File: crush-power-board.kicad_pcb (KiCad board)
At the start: 4 copper layers, 101.4 x 117.1 mm, 105 parts, among them J1 XT90PW-F, J2 1x2 Header, J3 Molex Micro Fit 3.0, J4 Barrel_Jack, J5 2157601008, U1 BD9G341AEFJ, U2 SIC461ED-T1-GE3, U3 SIC461ED-T1-GE3, U4 BD9G341AEFJ

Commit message: 3v3_t routing
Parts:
- moved R34 32.2 mm to (18.8, 41.1)
- moved R33 30.6 mm to (17.1, 42.8), turned to 0 degrees
- moved R35 28.8 mm to (19.9, 43.6), turned to 90 degrees
- moved C48 27.8 mm to (21.4, 68.8), turned to 90 degrees
- moved R38 25.1 mm to (31.3, 46.0), turned to 0 degrees
- moved R37 24.9 mm to (26.7, 44.6), turned to 180 degrees
- moved C46 22.9 mm to (17.1, 48.8), turned to 180 degrees
- moved R36 22.4 mm to (31.3, 47.6), turned to 0 degrees
- moved C45 20.8 mm to (16.4, 51.2), turned to -90 degrees
- moved L4 20.1 mm to (28.7, 66.3), turned to -90 degrees
- moved C47 19.6 mm to (28.1, 47.6), turned to 0 degrees
- moved U4 18.2 mm to (22.6, 48.2), turned to 180 degrees
- moved D6 3.73 mm to (25.8, 55.2), turned to 180 degrees
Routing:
- net +BATT_T: track 3.69 -> 65.0 mm, vias 0 -> 1
- net 3V3_T: track 47.1 -> 33.9 mm
- net Net-(D5-K): track 30.8 -> 18.0 mm
- net Net-(D6-K): track 30.6 -> 17.8 mm
- net Net-(U4-EN): track 0.36 -> 7.89 mm
- net GND1: track 0.00 -> 7.03 mm, vias 8 -> 9
- net 5V: vias 133 -> 127
- added copper zone on F.Cu, net +BATT_T
- added copper zone on F.Cu, net 3V3_T
- added copper zone on B.Cu, net GND1
- added copper zone on In1.Cu, net GND1
- added copper zone on In2.Cu, net GND1
- added copper zone on F.Cu, net Net-(D6-K)

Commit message: misc design fixes
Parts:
- moved R34 0.60 mm to (18.8, 40.5)
- moved C15 0.60 mm to (88.2, 34.2)
- moved C13 0.20 mm to (59.2, 63.1)
- moved R18 0.20 mm to (59.2, 60.5)
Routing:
- net 12V: track 201.2 -> 190.5 mm, vias 157 -> 247
- net Net-(U4-EN): track 7.89 -> 8.56 mm
- net GND: vias 1322 -> 1302
- net 5V: vias 127 -> 232
- net 3V3: vias 2 -> 52
- added copper zone on B.Cu, net 3V3

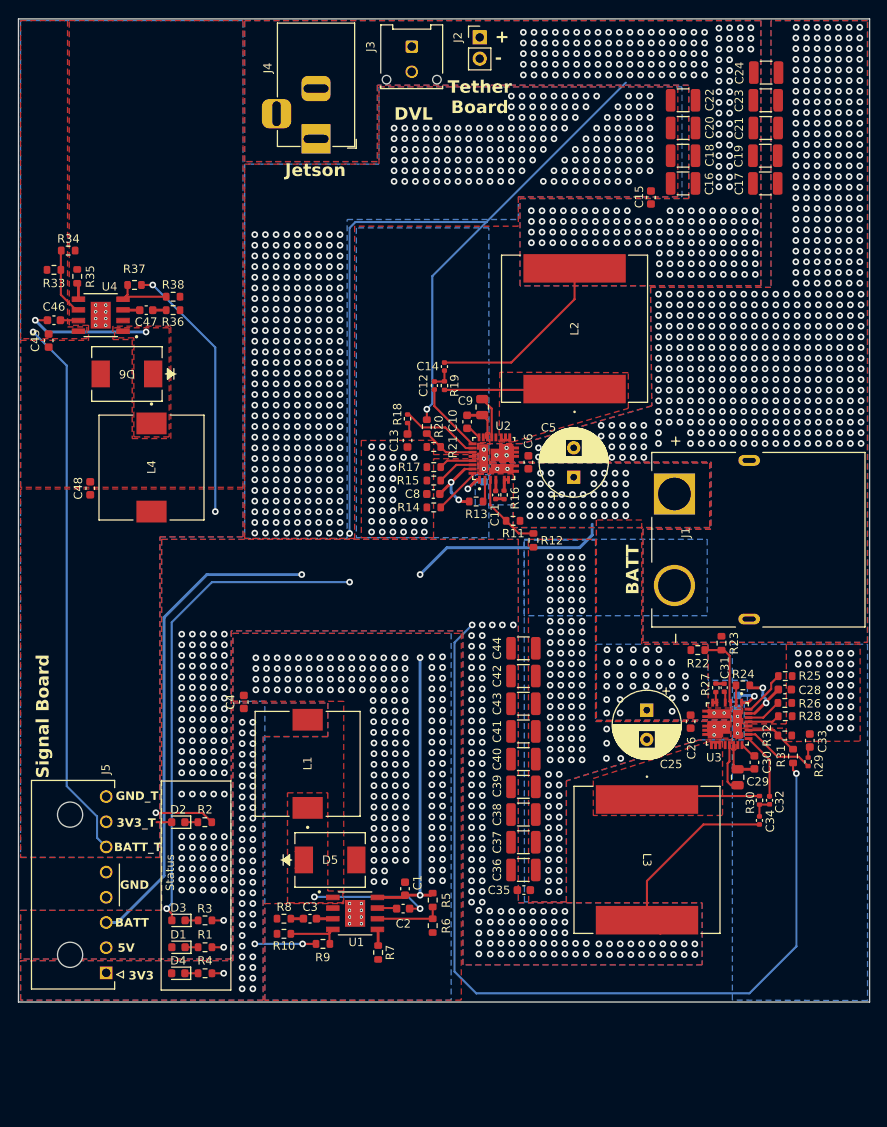
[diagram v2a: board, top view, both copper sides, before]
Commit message: fix silkscreen drc violations
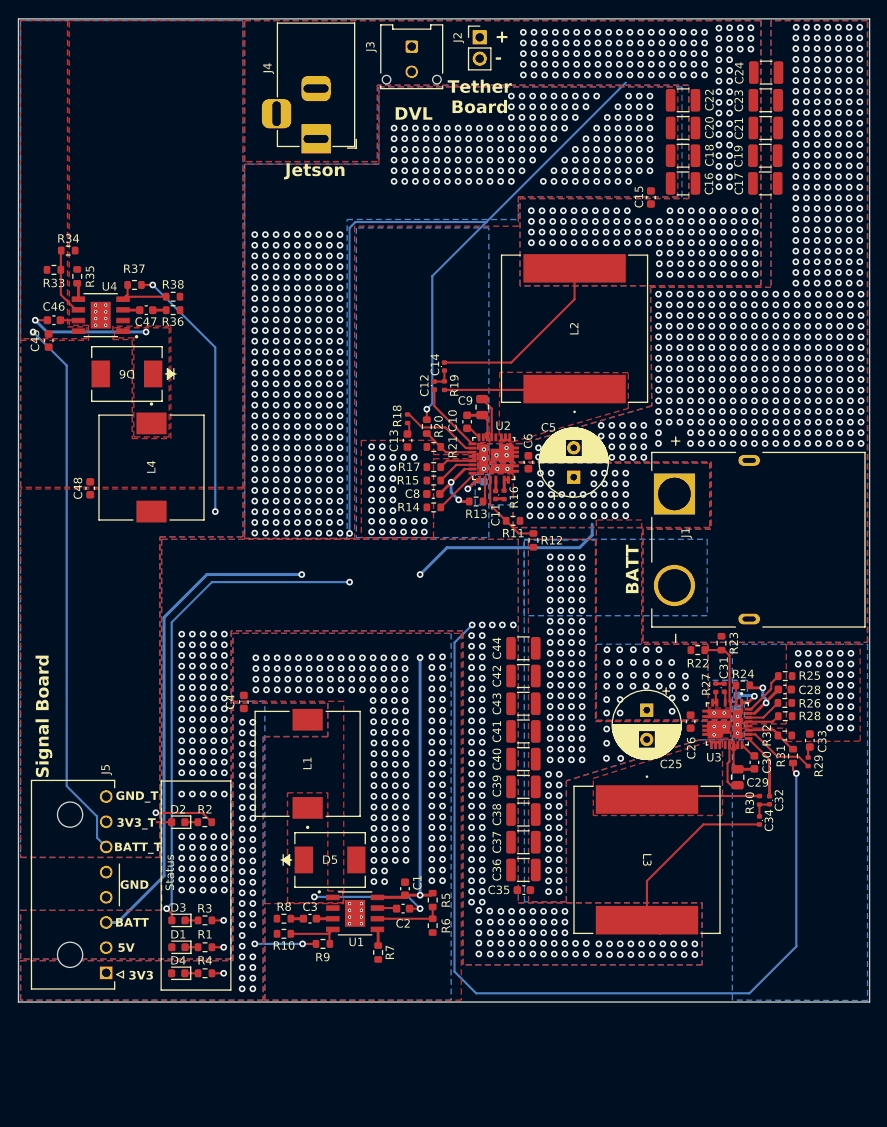
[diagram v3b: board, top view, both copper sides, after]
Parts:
- C11, C12, C14, C31, C32, C34: footprint Capacitor_SMD:C_0402_1005Metric -> crush-power-footprints:C_0402_1005Metric
- J4: footprint Connector_BarrelJack:BarrelJack_Horizontal -> crush-power-footprints:BarrelJack_Horizontal
- R16, R18, R19, R27, R29, R30: footprint Resistor_SMD:R_0402_1005Metric -> crush-power-footprints:R_0402_1005Metric
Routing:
- net Net-(U3-VSNS): track 8.11 -> 12.3 mm

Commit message: update board size
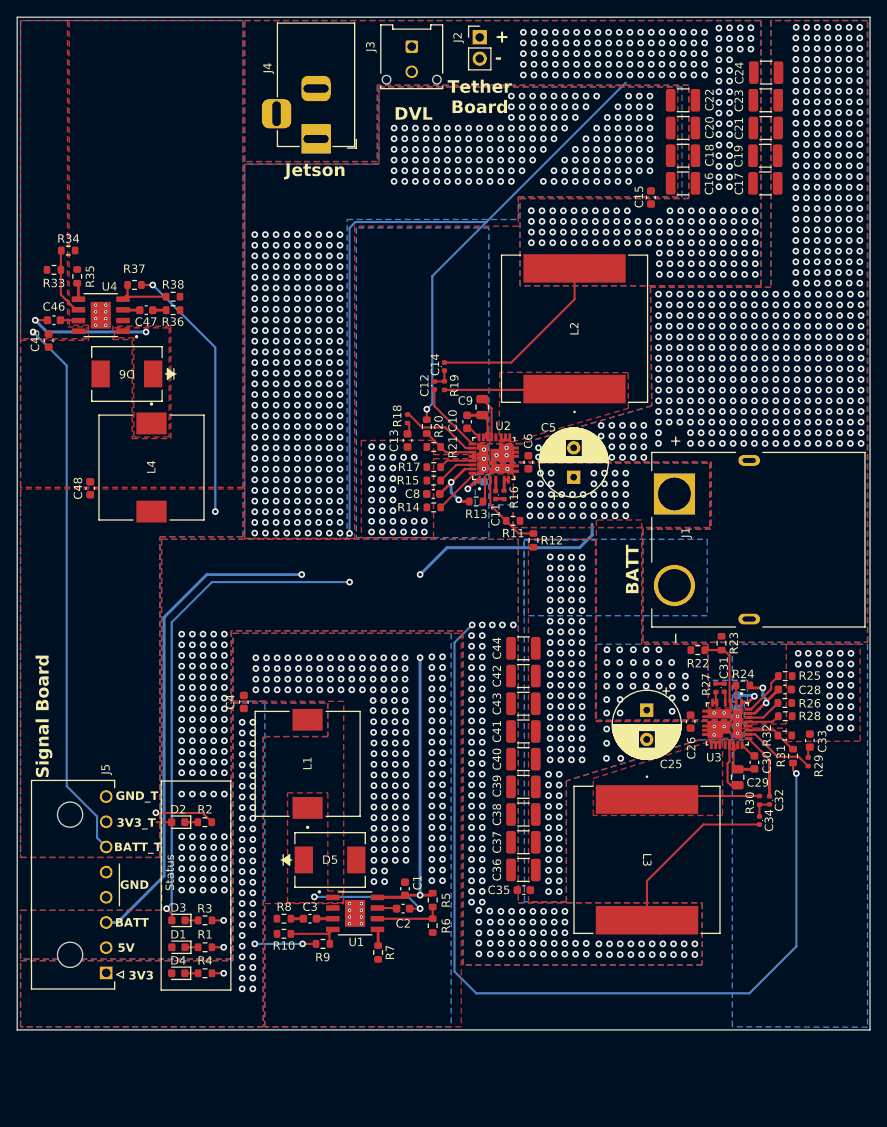
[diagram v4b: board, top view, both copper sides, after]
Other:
- board size 101.4 x 117.1 mm -> 101.6 x 120.6 mm
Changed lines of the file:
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@@
   (gr_rect (start 29.85 103.7) (end 38.15 128.6)
     (stroke (width 0.15) (type default)) (fill none) (layer "F.SilkS"))
-  (gr_rect (start 12.85 12.9) (end 114.25 130.025)
+  (gr_rect (start 12.7 12.7) (end 114.3 133.35)
     (stroke (width 0.1) (type default)) (fill none) (layer "Edge.Cuts"))
   (gr_text "Signal Board" (at 16.625 103.375 90) (layer "F.SilkS")
@@
     (polygon
       (pts
-        (xy 65.6 129.8)
-        (xy 42.2 129.823684)
+        (xy 65.6 132.975)
+        (xy 42.2 132.998684)
         (xy 42.2 118.3)
         (xy 51.6 118.3)
@@
         (xy 49.7 98.4)
         (xy 42 98.4)
-        (xy 42 129.8)
-        (xy 13.1 129.8)
+        (xy 42 132.975)
+        (xy 13.1 132.975)
         (xy 13.1 125.1)
         (xy 38.4 125.1)
@@
         (xy 114 87.2)
         (xy 97.7 87.2)
-        (xy 97.7 129.8)
-        (xy 13.1 129.8)
+        (xy 97.7 132.975)
+        (xy 13.1 132.975)
         (xy 13.1 113)
         (xy 29.9 113)
@@
         (xy 97.9 87.4)
         (xy 113.999781 87.4)
-        (xy 113.999985 129.85)
-        (xy 97.9 129.8)
+        (xy 113.999985 133.025)
+        (xy 97.9 132.975)
       )
     )
@@
         (xy 38.4 86.1)
         (xy 64.4 86.1)
-        (xy 64.4 129.8)
-        (xy 42.2 129.8)
+        (xy 64.4 132.975)
+        (xy 42.2 132.975)
       )
     )

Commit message: added mounting holes
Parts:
- added H1: MountingHole_Pad, MountingHole:MountingHole_4.3mm_M4_Pad_Via, F.Cu at (19.1, 19.1)
- added H2: MountingHole_Pad, MountingHole:MountingHole_4.3mm_M4_Pad_Via, F.Cu at (108.0, 19.1)
- added H3: MountingHole_Pad, MountingHole:MountingHole_4.3mm_M4_Pad_Via, F.Cu at (109.2, 134.6)
- added H4: MountingHole_Pad, MountingHole:MountingHole_4.3mm_M4_Pad_Via, F.Cu at (17.8, 134.6)
- moved C24 4.35 mm to (101.9, 23.6)
- moved C19 4.33 mm to (101.8, 33.5)
- moved C21 4.33 mm to (101.9, 30.2)
- moved C17 4.33 mm to (101.8, 36.8)
- moved C23 4.33 mm to (101.9, 26.9)
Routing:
- net GND: vias 1302 -> 1239
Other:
- board size 101.6 x 120.6 mm -> 101.6 x 127 mm

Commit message: fix mounting hole alignment
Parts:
- moved H4 2.29 mm to (19.1, 136.5)
- moved H3 2.29 mm to (108.0, 136.5)
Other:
- board size 101.6 x 127 mm -> 101.6 x 130.2 mm
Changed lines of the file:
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@@
   )
   (footprint "MountingHole:MountingHole_4.3mm_M4_Pad_Via" (layer "F.Cu")
-    (at 109.22 134.62)
+    (at 107.95 136.525)
     (descr "Mounting Hole 4.3mm, M4")
     (tags "mounting hole 4.3mm m4")
@@
   )
   (footprint "MountingHole:MountingHole_4.3mm_M4_Pad_Via" (layer "F.Cu")
-    (at 17.78 134.62)
+    (at 19.05 136.525)
     (descr "Mounting Hole 4.3mm, M4")
     (tags "mounting hole 4.3mm m4")
@@
   (gr_rect (start 29.85 103.7) (end 38.15 128.6)
     (stroke (width 0.15) (type default)) (fill none) (layer "F.SilkS"))
-  (gr_rect (start 12.7 12.7) (end 114.3 139.7)
+  (gr_rect (start 12.7 12.7) (end 114.3 142.875)
     (stroke (width 0.1) (type default)) (fill none) (layer "Edge.Cuts"))
   (gr_text "Signal Board" (at 16.625 103.375 90) (layer "F.SilkS")
@@
     (polygon
       (pts
-        (xy 65.6 139.325)
-        (xy 42.2 139.348684)
+        (xy 65.6 142.5)
+        (xy 42.2 142.523684)
         (xy 42.2 118.3)
         (xy 51.6 118.3)
@@
         (xy 49.7 98.4)
         (xy 42 98.4)
-        (xy 42 139.325)
-        (xy 13.1 139.325)
+        (xy 42 142.5)
+        (xy 13.1 142.5)
         (xy 13.1 125.1)
         (xy 38.4 125.1)
@@
         (xy 114 87.2)
         (xy 97.7 87.2)
-        (xy 97.7 139.325)
-        (xy 13.1 139.325)
+        (xy 97.7 142.5)
+        (xy 13.1 142.5)
         (xy 13.1 113)
         (xy 29.9 113)
@@
         (xy 97.9 87.4)
         (xy 113.999781 87.4)
-        (xy 113.999985 139.375)
-        (xy 97.9 139.325)
+        (xy 113.999985 142.55)
+        (xy 97.9 142.5)
       )
     )
@@
         (xy 38.4 86.1)
         (xy 64.4 86.1)
-        (xy 64.4 139.325)
-        (xy 42.2 139.325)
+        (xy 64.4 142.5)
+        (xy 42.2 142.5)
       )
     )

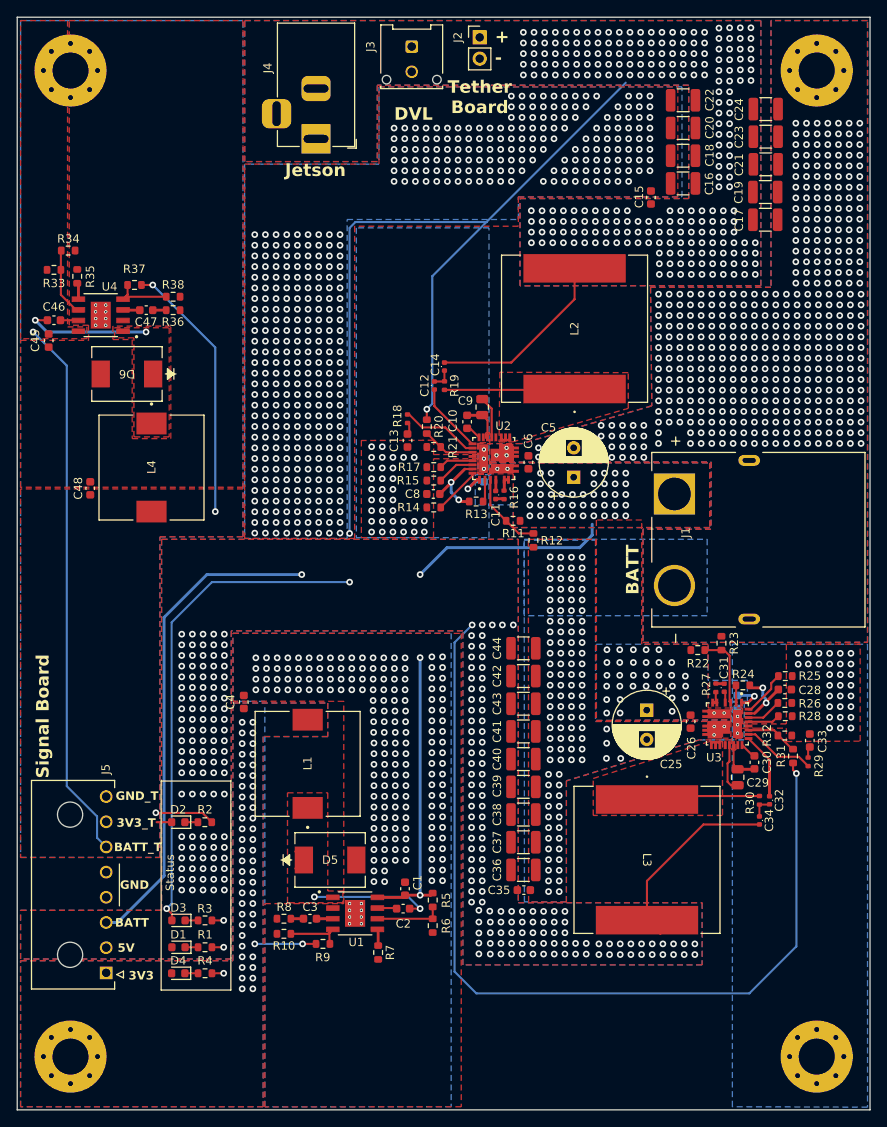
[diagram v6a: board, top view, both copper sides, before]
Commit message: increase 12v plane size
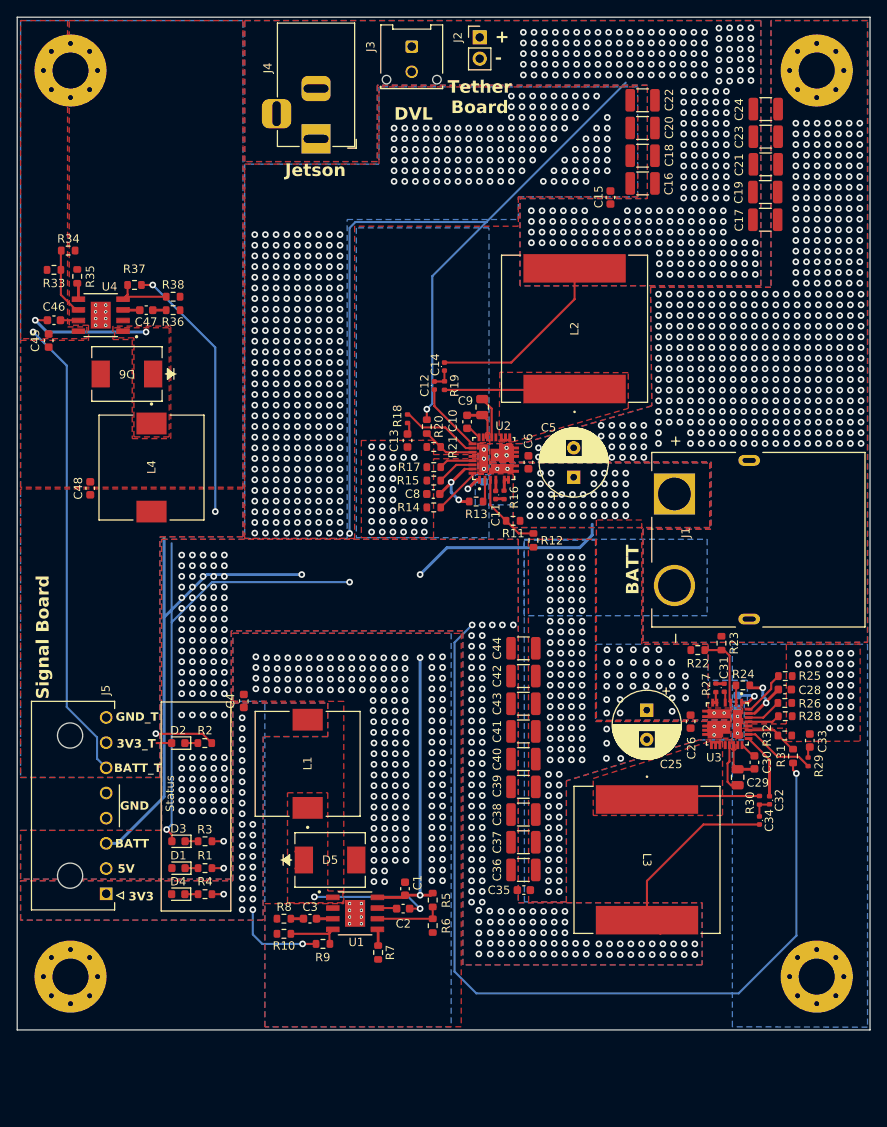
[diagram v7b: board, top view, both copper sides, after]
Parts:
- moved H3 9.53 mm to (108.0, 127.0)
- moved H4 9.53 mm to (19.1, 127.0)
- moved D1 9.42 mm to (31.9, 114.1)
- moved D2 9.42 mm to (31.9, 99.2)
- moved D3 9.42 mm to (31.9, 110.9)
- moved D4 9.42 mm to (31.9, 117.2)
- moved J5 9.42 mm to (23.3, 117.1)
- moved R1 9.42 mm to (35.1, 114.1)
- moved R2 9.42 mm to (35.0, 99.2)
- moved R3 9.42 mm to (35.1, 110.9)
- moved R4 9.42 mm to (35.1, 117.2)
- moved C15 4.83 mm to (83.4, 34.2)
- moved C16 4.83 mm to (87.2, 32.5)
- moved C18 4.83 mm to (87.2, 29.2)
- moved C20 4.83 mm to (87.2, 25.9)
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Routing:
- net +BATT_T: track 65.0 -> 55.5 mm
- net 3V3: track 7.30 -> 10.9 mm, vias 52 -> 29
- net 5V: track 131.7 -> 131.0 mm
- net 12V: vias 247 -> 279
- net GND: vias 1239 -> 1204
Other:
- board size 101.6 x 130.2 mm -> 101.6 x 120.6 mm
